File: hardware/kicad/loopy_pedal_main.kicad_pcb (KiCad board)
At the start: 2 copper layers, 82 x 88 mm, 84 parts, among them J1 USB_C_Receptacle_USB2.0_16P, J10 Conn_01x02, J11 Conn_01x03, J12 FSW_UNDO, J13 FSW_MODE, J14 FSW_TRACK1, J15 FSW_TRACK2, J16 FSW_TRACK3, J17 FSW_TRACK4, J18 FSW_CLEAR, J19 FSW_BANK, J2 Barrel_Jack, J3 FSW_RECPLAY, J4 FSW_STOP, J5 Conn_01x08, J6 Conn_02x03_Odd_Even, J7 Conn_02x03_Odd_Even, J8 MIDI_DIN5_RA, J9 MIDI_DIN5_RA, Q1 AO3401A, SW1 SW_Push, SW2 SW_Push, U1 ATmega328P-A, U10 74AHCT1G08, U2 ATmega16U2-A, U3 AP63203WU, U4 74AHCT1G125, U5 LM66100DCK, U6 LM66100DCK, U7 USBLC6-2SC6, U8 74AHCT1G125, U9 H11L1, Y1 16MHz, Y2 16MHz

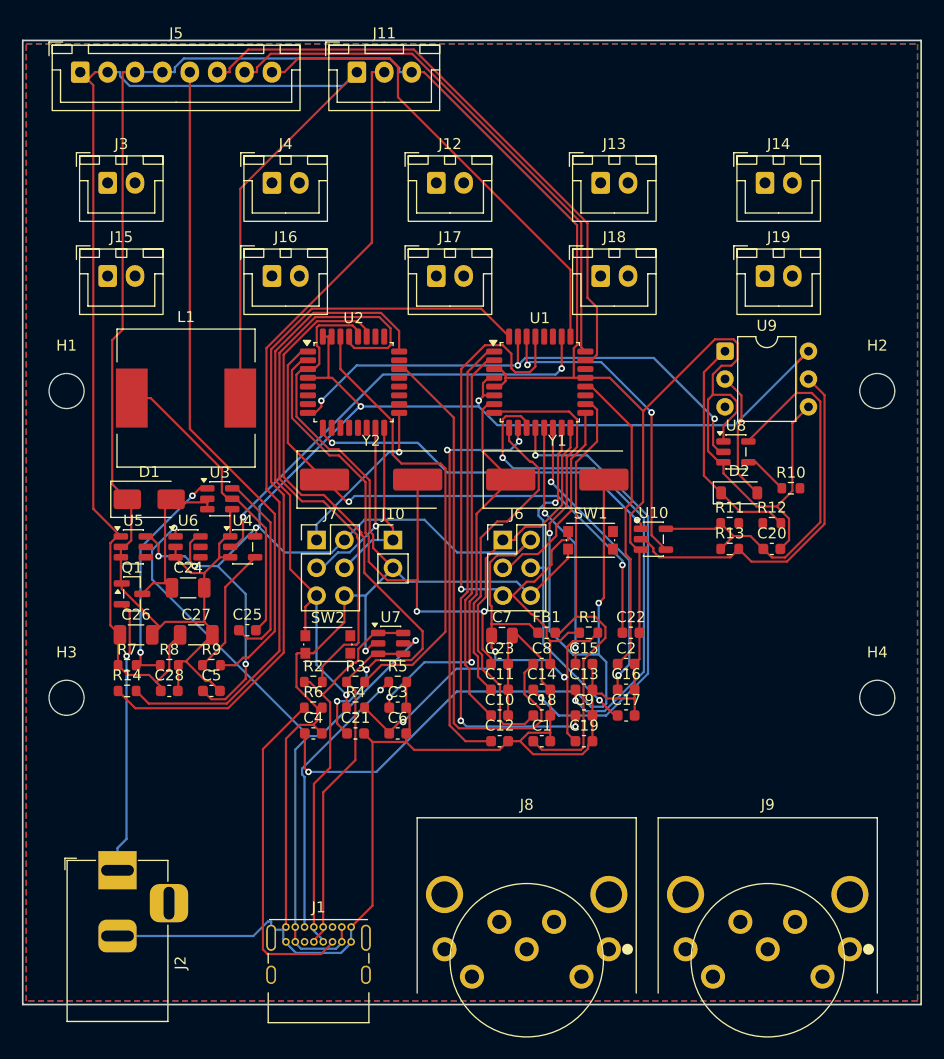
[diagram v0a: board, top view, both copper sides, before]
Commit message: refactor(pcb): compact + align main board, add footswitch silk labels
Shrink the main board 82x88 -> 82x84 mm: centre the 5x2 footswitch grid, widen
the logic zones into a 34->36 mm band, and move the four M3 mount holes to the
corners (bottom I/O re-spaced to clear them). Add a silkscreen function label
(RECPLAY, STOP, ... BANK) under each footswitch header. Re-routed; DRC 0 errors
/ 0 unconnected (remaining DRC items are silk-overlap/over-pour warnings inherent
to the dense layout).

Co-Authored-By: Claude Opus 4.8 <noreply@anthropic.com>
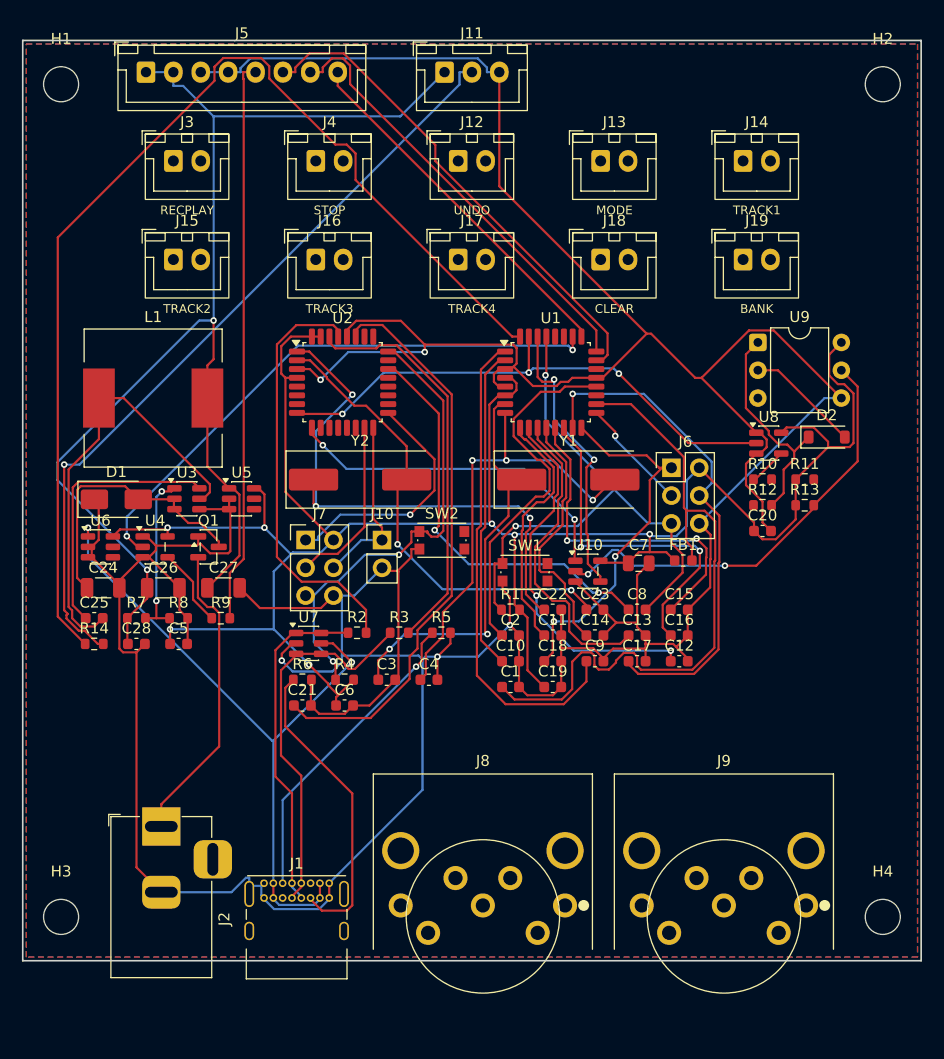
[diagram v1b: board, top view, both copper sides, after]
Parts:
- J12: value FSW_UNDO -> UNDO
- J13: value FSW_MODE -> MODE
- J14: value FSW_TRACK1 -> TRACK1
- J15: value FSW_TRACK2 -> TRACK2
- J16: value FSW_TRACK3 -> TRACK3
- J17: value FSW_TRACK4 -> TRACK4
- J18: value FSW_CLEAR -> CLEAR
- J19: value FSW_BANK -> BANK
- J3: value FSW_RECPLAY -> RECPLAY
- J4: value FSW_STOP -> STOP
- moved H1 28.0 mm to (33.5, 34.0)
- moved H2 28.0 mm to (108.5, 34.0)
- moved H3 20.0 mm to (33.5, 110.0)
- moved H4 20.0 mm to (108.5, 110.0)
- moved C12 18.0 mm to (89.9, 86.7)
- moved J6 16.7 mm to (89.2, 69.0)
- moved FB1 14.1 mm to (90.3, 77.5)
- moved C7 14.1 mm to (86.2, 77.7)
- moved SW2 14.1 mm to (68.3, 75.6)
- moved C25 14.0 mm to (36.5, 82.7)
- moved C4 11.6 mm to (67.1, 88.4)
- moved C2 10.9 mm to (74.5, 84.3)
- moved U5 10.8 mm to (50.0, 71.8)
- moved C15 10.0 mm to (89.9, 82.0)
- moved C8 10.0 mm to (86.1, 82.0)
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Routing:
- net N$4: track 89.1 -> 41.7 mm
- net +5V: track 233.2 -> 200.5 mm, vias 9 -> 7
- net IND_DATA: track 70.4 -> 100.5 mm
- net GND: track 457.5 -> 432.9 mm, vias 1 -> 5
- net SW_TRACK2: track 42.5 -> 23.1 mm, vias 2 -> 0
- net N$1: track 43.4 -> 61.3 mm
- net SW_TRACK1: track 44.9 -> 28.7 mm, vias 2 -> 0
- net N$9: track 54.3 -> 38.7 mm
- net SW_CLEAR: track 31.9 -> 46.5 mm, vias 2 -> 1
- net SW_NODE: track 28.1 -> 40.1 mm
- net DTR: track 49.4 -> 37.8 mm, vias 0 -> 2
- net RST_16: track 54.6 -> 43.3 mm, vias 1 -> 2
- net RING_DATA: track 41.2 -> 52.2 mm
- net ENC_SW: track 43.5 -> 33.4 mm
- net +9V: track 15.4 -> 25.5 mm
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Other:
- board size 82 x 88 mm -> 82 x 84 mm

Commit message: feat(pcb): silkscreen function labels on every connector and switch
Add on-silk function labels for all remaining I/O and headers (the footswitches
were already labelled): 9V, USB, MIDI OUT, MIDI IN, RING, IND, ICSP U1/U2, MOCO
(dualMoco mode jumper), and RST U1/U2. External ports read clearly; the in-logic
dev headers are labelled in place (tight against the dense packing). Silk-only
change - DRC 0 errors / 0 unconnected.

Co-Authored-By: Claude Opus 4.8 <noreply@anthropic.com>
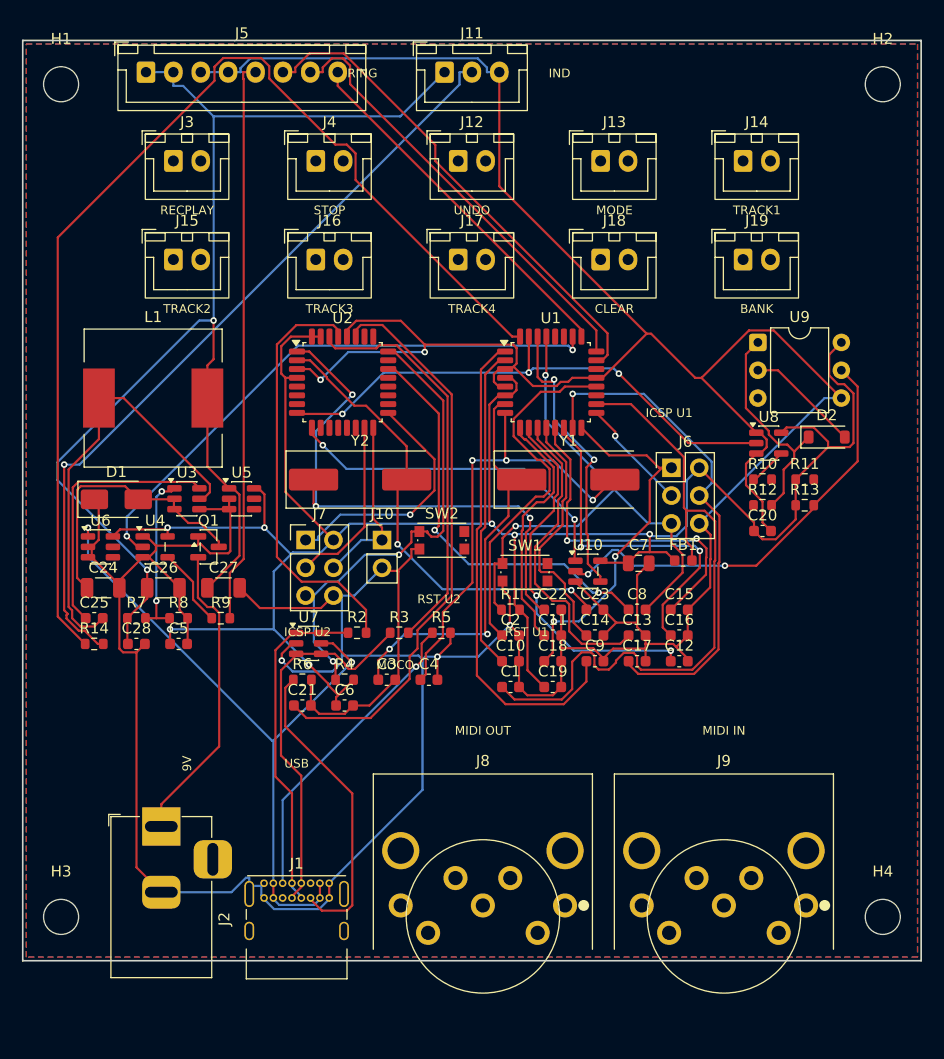
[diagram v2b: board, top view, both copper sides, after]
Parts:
- J1: value USB_C_Receptacle_USB2.0_16P -> USB
- J10: value Conn_01x02 -> MOCO
- J11: value Conn_01x03 -> IND
- J2: value Barrel_Jack -> 9V
- J5: value Conn_01x08 -> RING
- J6: value Conn_02x03_Odd_Even -> ICSP U1
- J7: value Conn_02x03_Odd_Even -> ICSP U2
- J8: value MIDI_DIN5_RA -> MIDI OUT
- J9: value MIDI_DIN5_RA -> MIDI IN
- SW1: value SW_Push -> RST U1
- SW2: value SW_Push -> RST U2
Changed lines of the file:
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@@
 			)
 		)
-		(property "Value" "Conn_01x08"
-			(at 8.75 4.6 0)
-			(layer "F.Fab")
+		(property "Value" "RING"
+			(at 19.75 0.105 0)
+			(layer "F.SilkS")
 			(effects
 				(font
-					(size 1 1)
-					(thickness 0.15)
+					(size 0.8 0.8)
+					(thickness 0.12)
 				)
 			)
@@
 			)
 		)
-		(property "Value" "SW_Push"
-			(at 0 2.55 0)
-			(layer "F.Fab")
+		(property "Value" "RST U2"
+			(at -0.255 5.375 0)
+			(layer "F.SilkS")
 			(effects
 				(font
-					(size 1 1)
-					(thickness 0.15)
+					(size 0.8 0.8)
+					(thickness 0.12)
 				)
 			)
@@
 			)
 		)
-		(property "Value" "Conn_02x03_Odd_Even"
-			(at 1.27 7.46 0)
-			(layer "F.Fab")
+		(property "Value" "ICSP U2"
+			(at 0.18 8.405 0)
+			(layer "F.SilkS")
 			(effects
 				(font
-					(size 1 1)
-					(thickness 0.15)
+					(size 0.8 0.8)
+					(thickness 0.12)
 				)
 			)
@@
 			)
 		)
-		(property "Value" "MIDI_DIN5_RA"
-			(at 0 5.5 0)
-			(layer "F.Fab")
+		(property "Value" "MIDI OUT"
+			(at 0 -15.955 0)
+			(layer "F.SilkS")
 			(effects
 				(font
-					(size 1 1)
-					(thickness 0.15)
+					(size 0.8 0.8)
+					(thickness 0.12)
 				)
 			)
@@
 			)
 		)
-		(property "Value" "USB_C_Receptacle_USB2.0_16P"
-			(at 2.975 9.925 0)
-			(layer "F.Fab")
+		(property "Value" "USB"
+			(at 2.975 -10.925 0)
+			(layer "F.SilkS")
 			(effects
 				(font
-					(size 1 1)
-					(thickness 0.15)
+					(size 0.8 0.8)
+					(thickness 0.12)
 				)
 			)
@@
 			)
 		)
-		(property "Value" "MIDI_DIN5_RA"
-			(at 0 5.5 0)
-			(layer "F.Fab")
+		(property "Value" "MIDI IN"
+			(at 0 -15.955 0)
+			(layer "F.SilkS")
 			(effects
 				(font
-					(size 1 1)
-					(thickness 0.15)
+					(size 0.8 0.8)
+					(thickness 0.12)
 				)
 			)
@@
 			)
 		)
-		(property "Value" "Conn_01x02"
-			(at 0 4.92 0)
-			(layer "F.Fab")
+		(property "Value" "MOCO"
+			(at 1.205 11.4 0)
+			(layer "F.SilkS")
 			(effects
 				(font
-					(size 1 1)
-					(thickness 0.15)
+					(size 0.8 0.8)
+					(thickness 0.12)
 				)
 			)
@@
 			)
 		)
-		(property "Value" "SW_Push"
-			(at 0 2.55 0)
-			(layer "F.Fab")
+		(property "Value" "RST U1"
+			(at 0.155 5.455 0)
+			(layer "F.SilkS")
 			(effects
 				(font
-					(size 1 1)
-					(thickness 0.15)
+					(size 0.8 0.8)
+					(thickness 0.12)
 				)
 			)
@@
 			)
 		)
-		(property "Value" "Conn_01x03"
-			(at 2.5 4.6 0)
-			(layer "F.Fab")
+		(property "Value" "IND"
+			(at 10.5 0.105 0)
+			(layer "F.SilkS")
 			(effects
 				(font
-					(size 1 1)
-					(thickness 0.15)
+					(size 0.8 0.8)
+					(thickness 0.12)
 				)
 			)
@@
 			)
 		)
-		(property "Value" "Conn_02x03_Odd_Even"
-			(at 1.27 7.46 0)
-			(layer "F.Fab")
+		(property "Value" "ICSP U1"
+			(at -0.21 -5.005 0)
+			(layer "F.SilkS")
 			(effects
 				(font
-					(size 1 1)
-					(thickness 0.15)
+					(size 0.8 0.8)
+					(thickness 0.12)
 				)
 			)
@@
 			)
 		)
-		(property "Value" "Barrel_Jack"
-			(at -6.2 -5.5 90)
-			(layer "F.Fab")
+		(property "Value" "9V"
+			(at 5.745 2.35 90)
+			(layer "F.SilkS")
 			(effects
 				(font
-					(size 1 1)
-					(thickness 0.15)
+					(size 0.8 0.8)
+					(thickness 0.12)
 				)
 			)
